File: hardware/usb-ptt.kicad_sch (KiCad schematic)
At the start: 0 parts

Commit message: Add provisional USB and isolated PTT circuit contract
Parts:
- added D100: TPD2EUSB30DRTR USB ESD protection, symbol TS700:PTT_Block
- added J100: USB-C receptacle / GCT USB4105 candidate, symbol TS700:PTT_Block
- added K100: AQY212GS PhotoMOS floating PTT closure, symbol TS700:PTT_Block
- added Q100: MMBT3904,215 PhotoMOS LED driver, symbol TS700:PTT_Block
- added U100: CP2102N-A02-GQFN24-R USB/UART bridge, symbol TS700:PTT_Block
- added U101: SN74LVC1G04 RTS inverter / default-off, symbol TS700:PTT_Block
- added U102: SN74LVC1G08 USB_READY AND REQUEST, symbol TS700:PTT_Block
- added U103: LTC6993-1 non-retriggerable 20.13 s limiter, symbol TS700:PTT_Block
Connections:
- new net: D100.1 (IN1), J100.3 (OUT1)
- new net: D100.2 (IN2), J100.4 (OUT2)
- new net: D100.3 (OUT1), U100.1 (IN1)
- new net: D100.4 (OUT2), U100.2 (IN2)
- new net: U100.4 (OUT2), U101.2 (IN2)
- new net: U102.4 (OUT2), U103.2 (IN2)
- new net: Q100.2 (IN2), U103.4 (OUT2)
- new net: K100.2 (IN2), Q100.4 (OUT2)
- no-connect marks 0 -> 16
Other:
- note added: "COMPUTER DOMAIN (USB_5V, COMPUTER_GND) FLOATING RADIO CLOSURE"
- note added: "D100 TPD2EUSB30DRTR: USB_D+ / USB_D− ESD clamp to COMPUTER_GND; R102/R103 22R series at U100."
- note added: "D101 + R111 separate computer-side PTT LED. TP100 USB_5V, TP101 COMPUTER_GND, TP102 REQUEST, TP103 DRIVE, TP104 PTT, TP105 PTT_RETURN."
- note added: "Default-off: /RTS pulled high R104 10k → U101 SN74LVC1G04 inverter → REQUEST; SUSPENDb pulled low R105 10k = USB_READY."
- note added: "Early release gates output immediately but does not reset U103; held request cannot retrigger after expiry. Timing/margins unmeasured."
- note added: "FLOATING RADIO-SIDE PHOTO-MOS OUTPUT: PTT, PTT_RETURN — intentionally no wire or ground across isolation"
- note added: "HOST / COMPUTER DOMAIN: USB_5V, COMPUTER_GND — USB-C, bridge, timer, driver and indicator return here"
- note added: "J100 USB-C receptacle candidate GCT USB4105-xx-A: VBUS=USB_5V; CC1/CC2 each R100/R101 5.1k to COMPUTER_GND."
- note added: "K100 Panasonic AQY212GS PhotoMOS candidate: output terminals connect ONLY PTT ↔ PTT_RETURN. No COMPUTER_GND connection."
- note added: "PROVISIONAL CAD-A01 / CAD-A02 — NOT FOR FABRICATION"
- note added: "Physical-finalization inputs: connector/ESD lands, host reset/suspend, radio PTT V/I/leakage, closure margin and timer bench evidence."
- note added: "Q100 MMBT3904,215: R108 1k base, R109 100k B-E; R110 470R USB_5V → K100 AQY212GS LED → collector."
- note added: "U100 CP2102N-A02-GQFN24-R: VREGIN=USB_5V; VDD=3V3; C100 1u + C101 100n; VBUS sense from USB_5V."
- note added: "U102 SN74LVC1G08 AND qualifies REQUEST with USB_READY. Reset, unpowered and suspend leave DRIVE low (CAD-A02)."
- note added: "U103 LTC6993-1 non-retriggerable limiter: DIVCODE=7, RSET=480k 1%, R106=1M/R107=887k 1%; 20.13 s nominal."
- note removed: "Do not join COMPUTER_GND to PTT or PTT_RETURN. Implement circuit and hierarchical labels in issue #15."
- note removed: "PROVISIONAL interface contract - circuit implementation pending"
- note removed: "Reference range: 100-199 — bridge, control, protection and isolated closure."
- note removed: "Root interface: COMPUTER_GND is host domain; PTT and PTT_RETURN are floating radio closure terminals."
- title: USB-C and isolated PTT -> USB-C serial and isolated PTT — PROVISIONAL

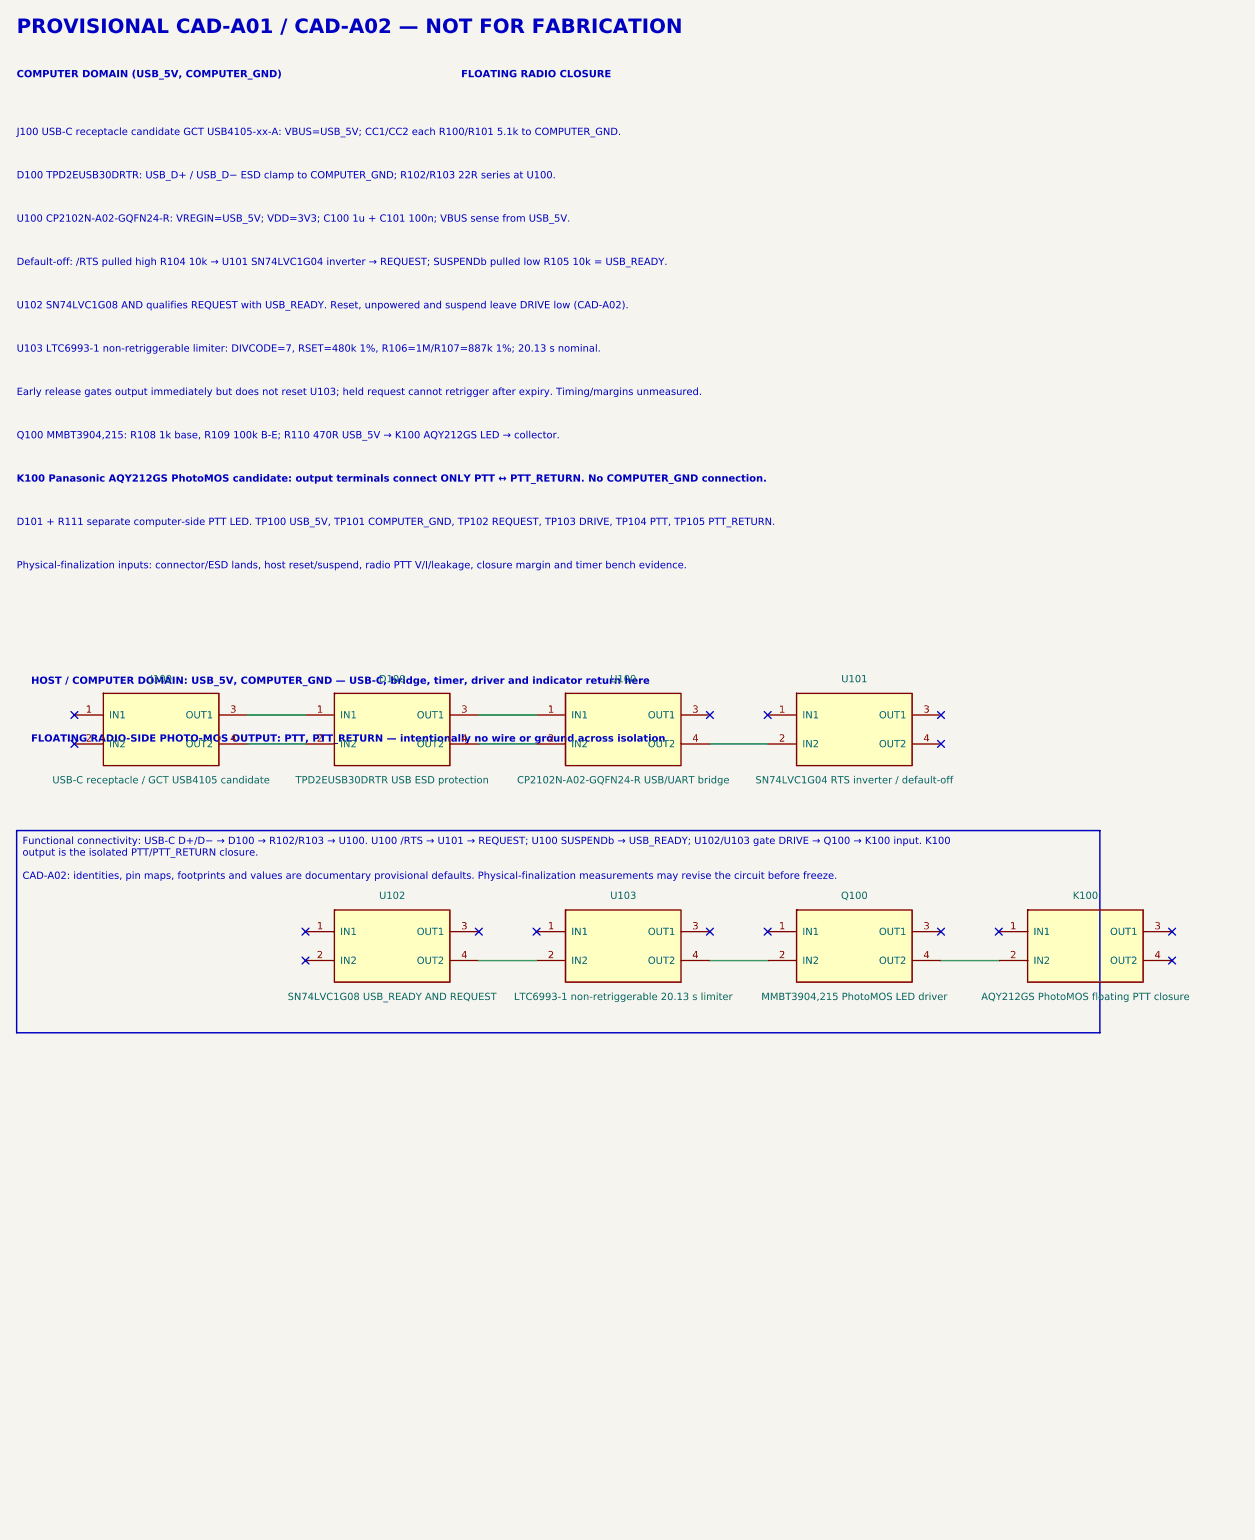
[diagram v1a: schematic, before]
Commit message: Use standard KiCad symbols for provisional USB PTT sheet
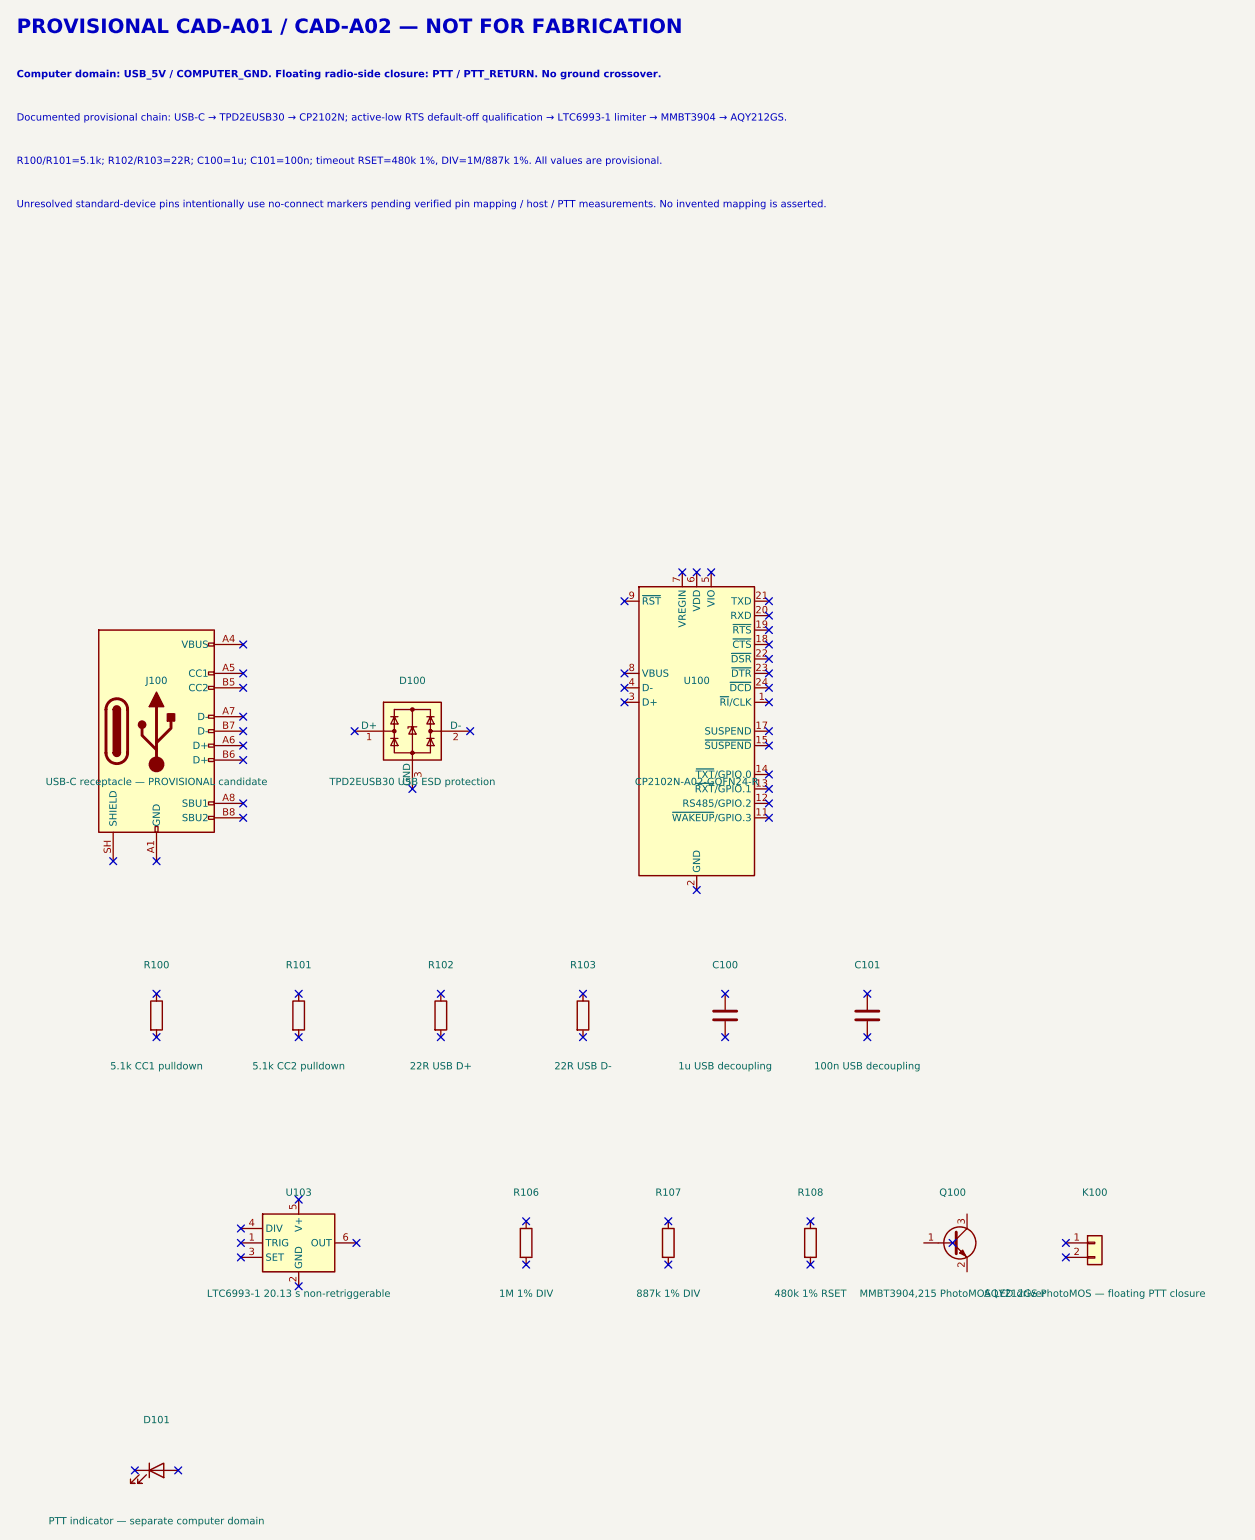
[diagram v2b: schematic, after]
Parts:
- removed D100: TPD2EUSB30DRTR USB ESD protection, symbol TS700:PTT_Block
- removed J100: USB-C receptacle / GCT USB4105 candidate, symbol TS700:PTT_Block
- removed K100: AQY212GS PhotoMOS floating PTT closure, symbol TS700:PTT_Block
- removed Q100: MMBT3904,215 PhotoMOS LED driver, symbol TS700:PTT_Block
- removed U100: CP2102N-A02-GQFN24-R USB/UART bridge, symbol TS700:PTT_Block
- removed U101: SN74LVC1G04 RTS inverter / default-off, symbol TS700:PTT_Block
- removed U102: SN74LVC1G08 USB_READY AND REQUEST, symbol TS700:PTT_Block
- removed U103: LTC6993-1 non-retriggerable 20.13 s limiter, symbol TS700:PTT_Block
- added C100: 1u USB decoupling, symbol Device:C
- added C101: 100n USB decoupling, symbol Device:C
- added D100: TPD2EUSB30 USB ESD protection, symbol Power_Protection:TPD2EUSB30
- added D101: PTT indicator — separate computer domain, symbol Device:LED
- added J100: USB-C receptacle — PROVISIONAL candidate, symbol Connector:USB_C_Receptacle_USB2.0_16P
- added K100: AQY212GS PhotoMOS — floating PTT closure, symbol Connector_Generic:Conn_01x02
- added Q100: MMBT3904,215 PhotoMOS LED driver, symbol Transistor_BJT:MMBT3904
- added R100: 5.1k CC1 pulldown, symbol Device:R
- added R101: 5.1k CC2 pulldown, symbol Device:R
- added R102: 22R USB D+, symbol Device:R
- added R103: 22R USB D-, symbol Device:R
- added R106: 1M 1% DIV, symbol Device:R
- added R107: 887k 1% DIV, symbol Device:R
- added R108: 480k 1% RSET, symbol Device:R
- added U100: CP2102N-A02-GQFN24-R, symbol Interface_USB:CP2102N-Axx-xQFN24
- added U103: LTC6993-1 20.13 s non-retriggerable, symbol Timer:LTC6993xS6-1
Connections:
- new net: J100.A1 (GND), J100.A12 (GND), J100.B1 (GND), J100.B12 (GND)
- new net: J100.A4 (VBUS), J100.A9 (VBUS), J100.B4 (VBUS), J100.B9 (VBUS)
- new net: U100.2 (GND), U100.25 (GND)
- no-connect marks 16 -> 65
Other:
- note added: "Computer domain: USB_5V / COMPUTER_GND. Floating radio-side closure: PTT / PTT_RETURN. No ground crossover."
- note added: "Documented provisional chain: USB-C → TPD2EUSB30 → CP2102N; active-low RTS default-off qualification → LTC6993-1 limiter → MMBT3904 → AQY212GS."
- note added: "R100/R101=5.1k; R102/R103=22R; C100=1u; C101=100n; timeout RSET=480k 1%, DIV=1M/887k 1%. All values are provisional."
- note added: "Unresolved standard-device pins intentionally use no-connect markers pending verified pin mapping / host / PTT measurements. No invented mapping is asserted."
- note removed: "COMPUTER DOMAIN (USB_5V, COMPUTER_GND) FLOATING RADIO CLOSURE"
- note removed: "D100 TPD2EUSB30DRTR: USB_D+ / USB_D− ESD clamp to COMPUTER_GND; R102/R103 22R series at U100."
- note removed: "D101 + R111 separate computer-side PTT LED. TP100 USB_5V, TP101 COMPUTER_GND, TP102 REQUEST, TP103 DRIVE, TP104 PTT, TP105 PTT_RETURN."
- note removed: "Default-off: /RTS pulled high R104 10k → U101 SN74LVC1G04 inverter → REQUEST; SUSPENDb pulled low R105 10k = USB_READY."
- note removed: "Early release gates output immediately but does not reset U103; held request cannot retrigger after expiry. Timing/margins unmeasured."
- note removed: "FLOATING RADIO-SIDE PHOTO-MOS OUTPUT: PTT, PTT_RETURN — intentionally no wire or ground across isolation"
- note removed: "HOST / COMPUTER DOMAIN: USB_5V, COMPUTER_GND — USB-C, bridge, timer, driver and indicator return here"
- note removed: "J100 USB-C receptacle candidate GCT USB4105-xx-A: VBUS=USB_5V; CC1/CC2 each R100/R101 5.1k to COMPUTER_GND."
- note removed: "K100 Panasonic AQY212GS PhotoMOS candidate: output terminals connect ONLY PTT ↔ PTT_RETURN. No COMPUTER_GND connection."
- note removed: "Physical-finalization inputs: connector/ESD lands, host reset/suspend, radio PTT V/I/leakage, closure margin and timer bench evidence."
- note removed: "Q100 MMBT3904,215: R108 1k base, R109 100k B-E; R110 470R USB_5V → K100 AQY212GS LED → collector."
- note removed: "U100 CP2102N-A02-GQFN24-R: VREGIN=USB_5V; VDD=3V3; C100 1u + C101 100n; VBUS sense from USB_5V."
- note removed: "U102 SN74LVC1G08 AND qualifies REQUEST with USB_READY. Reset, unpowered and suspend leave DRIVE low (CAD-A02)."
- note removed: "U103 LTC6993-1 non-retriggerable limiter: DIVCODE=7, RSET=480k 1%, R106=1M/R107=887k 1%; 20.13 s nominal."
